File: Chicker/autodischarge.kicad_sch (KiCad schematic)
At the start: 10 parts, among them Q5 TN2130K1-G, Q6 IPD60R3K4CEAUMA1, Q8 TN2130K1-G

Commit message: chicker modifications (mostly ready to order)
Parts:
- renumbered R9 to R31, R9 to R32, R9 to R33, R9 to R34

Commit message: ESD+schematic fixes
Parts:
- D12: value 3SMBJ5929B-TP -> 3SMBJ5929B-TP
- Q5, Q8: value TN2130K1-G -> TN2130K1-G

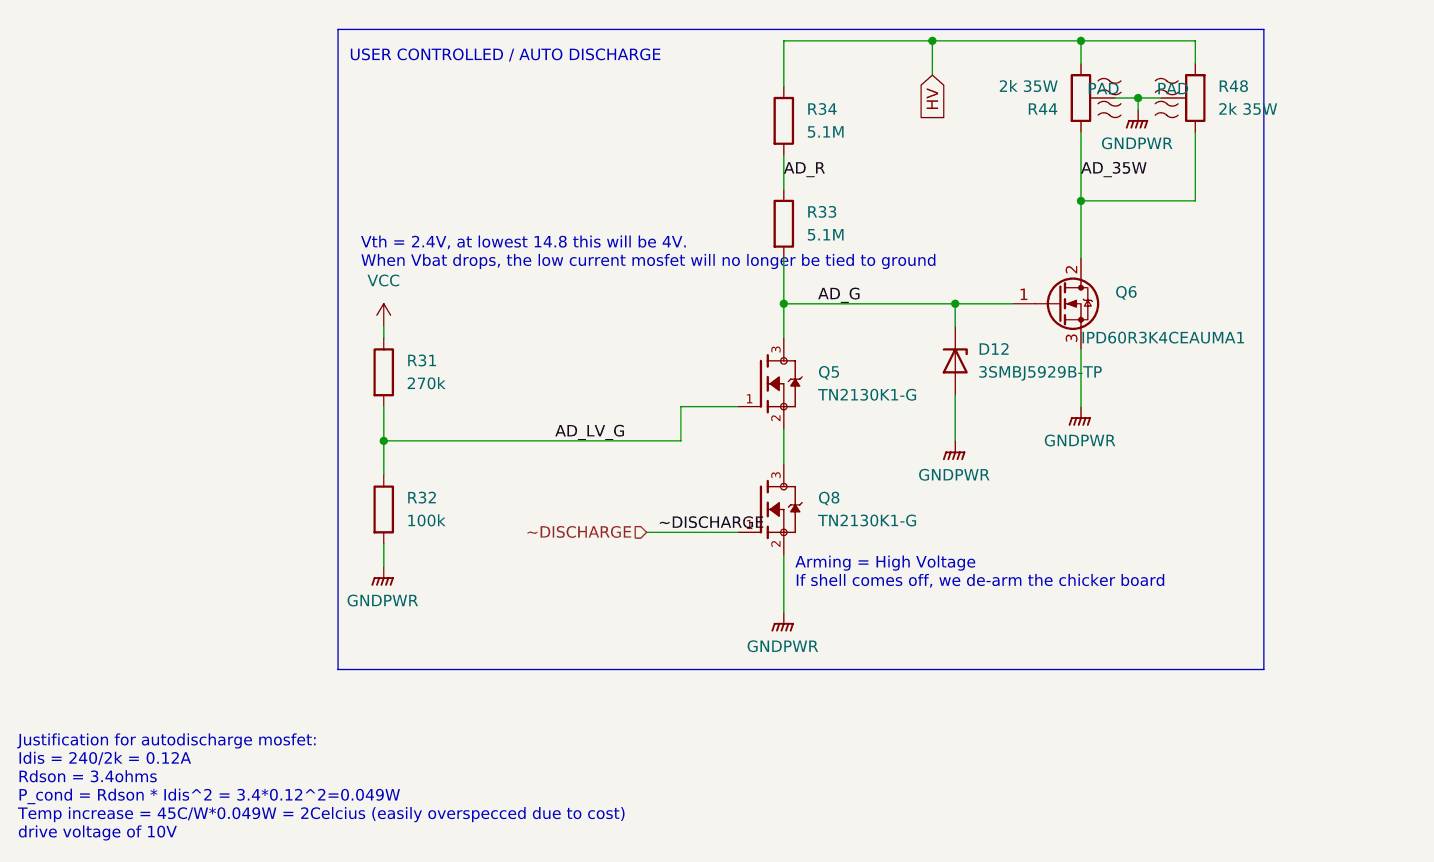
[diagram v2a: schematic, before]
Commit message: changed more to basic
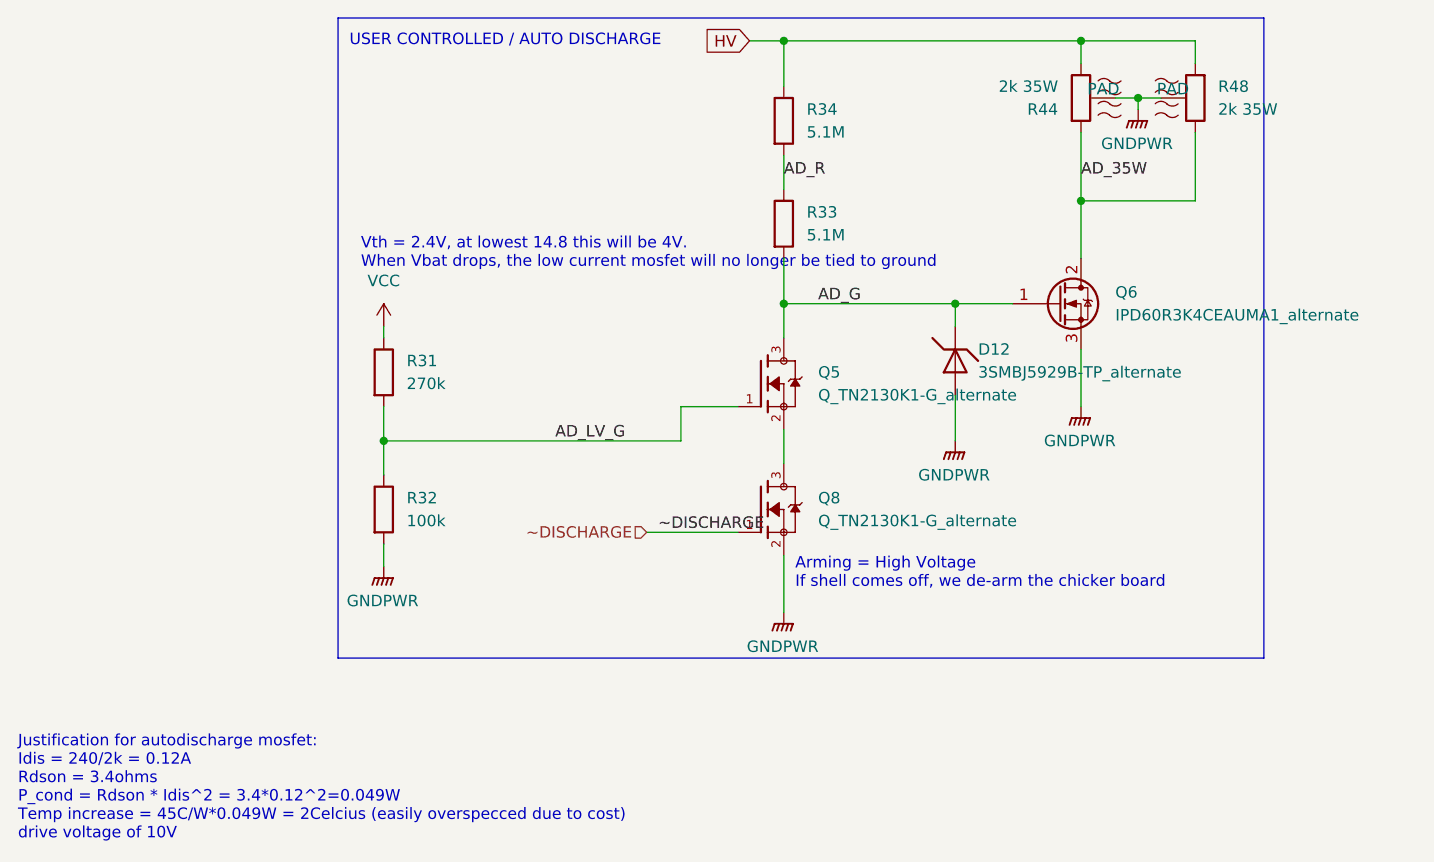
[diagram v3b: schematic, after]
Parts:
- removed D12: 3SMBJ5929B-TP, bots:D_SMB, symbol bots:D_ZENER_3SMBJ5929B-TP
- removed Q5, Q8: TN2130K1-G, bots:SOT95P240X111-3N, symbol bots:TN2130K1-G
- removed Q6: IPD60R3K4CEAUMA1, bots:DPAK-3_ONS, symbol bots:IPD60R3K4CEAUMA1
- added D12: 3SMBJ5929B-TP_alternate, bots:D_SMB, symbol bots:D_ZENER_3SMBJ5929B-TP_alternate
- added Q5, Q8: Q_TN2130K1-G_alternate, bots:SOT95P240X111-3N, symbol bots:Q_TN2130K1-G_alternate
- added Q6: IPD60R3K4CEAUMA1_alternate, bots:DPAK-3_ONS, symbol bots:Q_IPD60R3K4CEAUMA1_alternate
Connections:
- net AD_35W: now also Q6.2 (D)
- net AD_G: now also D12.1 (K), Q5.3, Q6.1 (G)
- net AD_LV_G: now also Q5.1
- net GNDPWR: now also D12.2 (A), Q6.3 (S), Q8.2
- net ~DISCHARGE: now also Q8.1
- new net: Q5.2, Q8.3
